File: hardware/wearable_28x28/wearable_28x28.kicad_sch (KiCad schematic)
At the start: 0 parts

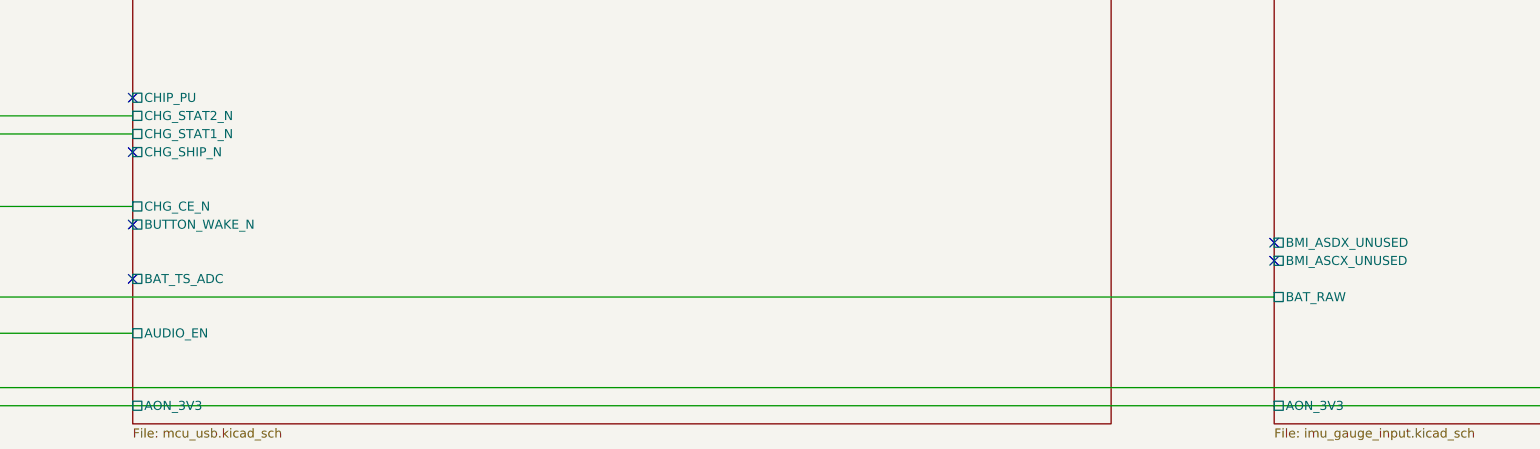
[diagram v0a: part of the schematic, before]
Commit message: Regenerate hierarchies with selected EVT parts
Co-authored-by: illiapliukhin <illiapliukhin@users.noreply.github.com>
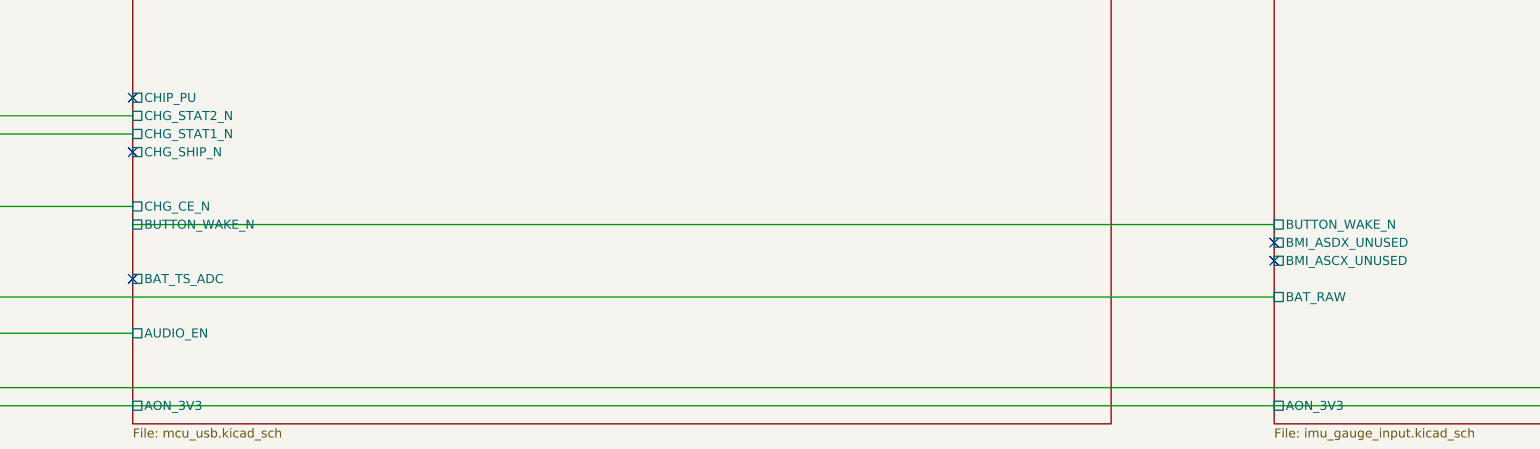
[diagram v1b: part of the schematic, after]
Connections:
- no-connect marks 118 -> 117
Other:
- sheet IMU_Gauge_Input ports: added BUTTON_WAKE_N; removed none
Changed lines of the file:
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@@
-	)
-	(no_connect
-		(at 180.34 662.94)
 	)
 	(no_connect
@@
 		(pts
 			(xy 660.4 563.88) (xy 980.44 563.88)
+		)
+		(stroke
+			(width 0)
+			(type default)
+		)
+	)
+	(wire
+		(pts
+			(xy 180.34 662.94) (xy 340.36 662.94)
 		)
 		(stroke
@@
 			(effects
 				(font
+					(size 1.27 1.27)
+				)
+				(justify left)
+			)
+		)
+		(pin "BUTTON_WAKE_N" passive
+			(at 340.36 662.94 180)
+			(effects
+				(font
